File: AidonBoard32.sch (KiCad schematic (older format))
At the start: 30 parts, among them J1 RJ12, M1 MICRO_USB_18_TH, Q1 S8050, Q2 S8050, U1 AMS1117-3V3, U2 CP2102N-GQFN24, U3 ESP32-WROOM, U4 74HC04D

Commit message: Finished first revision of AidonBoard32!
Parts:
- added D6: 1N5819, Diode_SMD:D_SOD-123F, symbol Diode:1N5819
- D1: value 1N5819/SS14 -> 1N5819
- U4: footprint Package_SO:SO-14_3.9x8.65mm_P1.27mm -> Package_SO:SOIC-14_3.9x8.7mm_P1.27mm
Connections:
- net labels added: +5V, HAN_OUT, VDD
- net labels removed: UART_TX
- wire segments 128 -> 147
- no-connect marks 37 -> 50
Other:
- note added: "ESP32 Flashing"
- note added: "LEDs"
- note added: "P1 Port"
- note added: "RJ11 Connector"
- note removed: "HAN Port - UART"
- note removed: "LED"
- note removed: "Programming"
- note removed: "RJ Connector"
- moved on the sheet: C1, C10, C2, C3, C4, C5, C6, C7, D2, D3, D4, D5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

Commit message: Update
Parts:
- removed D1, D6: 1N5819, Diode_SMD:D_SOD-123F, symbol Diode:1N5819
- removed U4: 74HC04D, Package_SO:SOIC-14_3.9x8.7mm_P1.27mm, symbol Henrik-IC-Inverters:74HC04D
- added D1: SS54, Diode_SMD:D_SMA, symbol Diode:B120-E3
- added D5: LED_Small, LED_SMD:LED_0603_1608Metric_Pad1.05x0.95mm_HandSolder, symbol Device:LED_Small
- added Q1: Si2301CDS-T1-GE3, Package_TO_SOT_SMD:SOT-23_Handsoldering, symbol Device:Q_PMOS_GSD
- added Q4: MMBT3904, Package_TO_SOT_SMD:SOT-23_Handsoldering, symbol Transistor_BJT:MMBT3904
- added R1: 100K, Resistor_SMD:R_0603_1608Metric_Pad0.98x0.95mm_HandSolder, symbol Device:R_Small
- added R10, R12: 10K, Resistor_SMD:R_0603_1608Metric_Pad0.98x0.95mm_HandSolder, symbol Device:R_Small
- added R11: 1K, Resistor_SMD:R_0603_1608Metric_Pad0.98x0.95mm_HandSolder, symbol Device:R_Small
- added R9: 220, Resistor_SMD:R_0603_1608Metric_Pad0.98x0.95mm_HandSolder, symbol Device:R_Small
- C1, C2: Description (none) -> Power Regulator Capacitors; LCSC (none) -> C231297
- C10: renamed from C7; footprint Capacitor_SMD:C_1206_3216Metric_Pad1.33x1.80mm_HandSolder -> Capacitor_SMD:C_0603_1608Metric_Pad1.08x0.95mm_HandSolder; Description (none) -> Various Capacitors; LCSC (none) -> C478888
- C3, C5: Description (none) -> CP2102N Capacitors; LCSC (none) -> C129235
- C4, C6: footprint Capacitor_SMD:C_1206_3216Metric_Pad1.33x1.80mm_HandSolder -> Capacitor_SMD:C_0603_1608Metric_Pad1.08x0.95mm_HandSolder; Description (none) -> Various Capacitors; LCSC (none) -> C478888
- C7: renamed from C8; value 47uF -> 10uF; Description (none) -> ESP32 VDD Capacitor; LCSC (none) -> C119052
- C8: renamed from C9; footprint Capacitor_SMD:C_1206_3216Metric_Pad1.33x1.80mm_HandSolder -> Capacitor_SMD:C_0603_1608Metric_Pad1.08x0.95mm_HandSolder; Description (none) -> Various Capacitors; LCSC (none) -> C478888
- C9: renamed from C10; value 10uF -> 1uF; Description (none) -> ESP32 EN PIN Capacitor; LCSC (none) -> C123716
- D2: footprint LED_SMD:LED_1206_3216Metric_Pad1.42x1.75mm_HandSolder -> LED_SMD:LED_0603_1608Metric_Pad1.05x0.95mm_HandSolder; Description (none) -> TX LED / Blue; LCSC (none) -> C273617
- D3: footprint LED_SMD:LED_1206_3216Metric_Pad1.42x1.75mm_HandSolder -> LED_SMD:LED_0603_1608Metric_Pad1.05x0.95mm_HandSolder; Description (none) -> RX LED / Yellow; LCSC (none) -> C192668
- D4: footprint LED_SMD:LED_1206_3216Metric_Pad1.42x1.75mm_HandSolder -> LED_SMD:LED_0603_1608Metric_Pad1.05x0.95mm_HandSolder; Description (none) -> Power LED / Red; LCSC (none) -> C192315
- D6: renamed from D5; Description (none) -> RGB LED; LCSC (none) -> C114586
- J1: footprint Henrik-Connectors:RJ11-6 -> 5555165-1:TE_5555165-1; Description (none) -> RJ12 Connector; LCSC (none) -> C305981
- M1: value MICRO_USB_18_TH -> U-F-M5DD-Y-L; Description (none) -> Micro USB Connector; LCSC (none) -> C91146
- Q2: renamed from Q1; value S8050 -> MMBT3904; LCSC (none) -> C20526
- Q3: renamed from Q2; value S8050 -> MMBT3904; LCSC (none) -> C20526
- R2: renamed from R1; value 1k -> 1K; footprint Resistor_SMD:R_1206_3216Metric_Pad1.30x1.75mm_HandSolder -> Resistor_SMD:R_0603_1608Metric_Pad0.98x0.95mm_HandSolder; LCSC (none) -> C491209
- R3: renamed from R7; value 1k -> 10K; footprint Resistor_SMD:R_1206_3216Metric_Pad1.30x1.75mm_HandSolder -> Resistor_SMD:R_0603_1608Metric_Pad0.98x0.95mm_HandSolder; LCSC (none) -> C510087
- R4: renamed from R5; value 12k -> 10K; footprint Resistor_SMD:R_1206_3216Metric_Pad1.30x1.75mm_HandSolder -> Resistor_SMD:R_0603_1608Metric_Pad0.98x0.95mm_HandSolder; LCSC (none) -> C510087
- R5: renamed from R6; value 12k -> 10K; footprint Resistor_SMD:R_1206_3216Metric_Pad1.30x1.75mm_HandSolder -> Resistor_SMD:R_0603_1608Metric_Pad0.98x0.95mm_HandSolder; LCSC (none) -> C510087
- R6: renamed from R2; value 1k -> 220; footprint Resistor_SMD:R_1206_3216Metric_Pad1.30x1.75mm_HandSolder -> Resistor_SMD:R_0603_1608Metric_Pad0.98x0.95mm_HandSolder; Description (none) -> LED Resistors; LCSC (none) -> C441917
- R7: renamed from R3; value 1k -> 220; footprint Resistor_SMD:R_1206_3216Metric_Pad1.30x1.75mm_HandSolder -> Resistor_SMD:R_0603_1608Metric_Pad0.98x0.95mm_HandSolder; Description (none) -> LED Resistors; LCSC (none) -> C441917
- R8: renamed from R4; value 1k -> 220; footprint Resistor_SMD:R_1206_3216Metric_Pad1.30x1.75mm_HandSolder -> Resistor_SMD:R_0603_1608Metric_Pad0.98x0.95mm_HandSolder; Description (none) -> LED Resistors; LCSC (none) -> C441917
- U1: LCSC (none) -> C6186
- U2: LCSC (none) -> C1550551
- U3: LCSC (none) -> C82899
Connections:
- net labels added: VCC
- net labels removed: VDD
- wire segments 147 -> 156
- no-connect marks 50 -> 39
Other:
- note added: "P1 Signal Inversion"
- note removed: "P1 Port"
- moved on the sheet: C1, C2, D2, D3, D4, Q2, Q3, R6, R7, R8, U1

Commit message: Fixed routing
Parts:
- J1: symbol Connector:RJ12 -> AidonBoard32-rescue:RJ12-Connector
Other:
- moved on the sheet: R6, R7, R8, R9
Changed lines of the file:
@@
 $EndComp
-Wire Wire Line
-	9450 2350 9450 2100
-Wire Wire Line
-	9450 1900 9450 1800
 Wire Wire Line
 	9450 2350 9650 2350
@@
 $EndComp
 $Comp
-L Connector:RJ12 J1
+L AidonBoard32-rescue:RJ12-Connector J1
 U 1 1 608CEFE8
 P 4250 4300
@@
 $EndComp
 $Comp
-L Device:R_Small R10
-U 1 1 60C4F049
-P 9450 2000
-F 0 "R10" H 9456 2123 50  0000 L CNN
-F 1 "10K" H 9459 1889 50  0000 L CNN
-F 2 "Resistor_SMD:R_0603_1608Metric_Pad0.98x0.95mm_HandSolder" H 9450 2000 50  0001 C CNN
-F 3 "https://datasheet.lcsc.com/lcsc/2004232132_ROHM-Semicon-ESR03EZPF1002_C510087.pdf" H 9450 2000 50  0001 C CNN
-F 4 "C510087" H 9450 2000 50  0001 C CNN "LCSC"
-	1    9450 2000
-	1    0    0    -1
-$EndComp
-$Comp
 L Device:R_Small R11
 U 1 1 60C63B88
@@
 L Device:R_Small R8
 U 1 1 5AAA8BC7
-P 9250 4450
-F 0 "R8" V 9176 4403 50  0000 L CNN
-F 1 "220" V 9325 4377 50  0000 L CNN
-F 2 "Resistor_SMD:R_0603_1608Metric_Pad0.98x0.95mm_HandSolder" H 9250 4450 50  0001 C CNN
-F 3 "" H 9250 4450 50  0001 C CNN
-F 4 "C441917" H 9250 4450 50  0001 C CNN "LCSC"
-F 5 "LED Resistors" H 9250 4450 50  0001 C CNN "Description"
-	1    9250 4450
-	0    1    1    0
-$EndComp
-Wire Wire Line
-	9500 4450 9350 4450
-Wire Wire Line
-	9050 4450 9150 4450
+P 9200 4450
+F 0 "R8" V 9126 4403 50  0000 L CNN
+F 1 "220" V 9275 4377 50  0000 L CNN
+F 2 "Resistor_SMD:R_0603_1608Metric_Pad0.98x0.95mm_HandSolder" H 9200 4450 50  0001 C CNN
+F 3 "" H 9200 4450 50  0001 C CNN
+F 4 "C441917" H 9200 4450 50  0001 C CNN "LCSC"
+F 5 "LED Resistors" H 9200 4450 50  0001 C CNN "Description"
+	1    9200 4450
+	0    1    1    0
+$EndComp
+Wire Wire Line
+	9450 4450 9300 4450
+Wire Wire Line
+	9050 4450 9100 4450
 $Comp
 L Device:LED_Small D4
@@
 L Device:R_Small R9
 U 1 1 60FFD57F
-P 9250 4700
-F 0 "R9" V 9173 4653 50  0000 L CNN
-F 1 "220" V 9328 4637 50  0000 L CNN
-F 2 "Resistor_SMD:R_0603_1608Metric_Pad0.98x0.95mm_HandSolder" H 9250 4700 50  0001 C CNN
-F 3 "" H 9250 4700 50  0001 C CNN
-F 4 "C441917" H 9250 4700 50  0001 C CNN "LCSC"
-F 5 "LED Resistors" H 9250 4700 50  0001 C CNN "Description"
-	1    9250 4700
-	0    1    1    0
-$EndComp
-Wire Wire Line
-	9050 4700 9150 4700
-Wire Wire Line
-	9500 4700 9350 4700
+P 9200 4700
+F 0 "R9" V 9123 4653 50  0000 L CNN
+F 1 "220" V 9278 4637 50  0000 L CNN
+F 2 "Resistor_SMD:R_0603_1608Metric_Pad0.98x0.95mm_HandSolder" H 9200 4700 50  0001 C CNN
+F 3 "" H 9200 4700 50  0001 C CNN
+F 4 "C441917" H 9200 4700 50  0001 C CNN "LCSC"
+F 5 "LED Resistors" H 9200 4700 50  0001 C CNN "Description"
+	1    9200 4700
+	0    1    1    0
+$EndComp
+Wire Wire Line
+	9050 4700 9100 4700
+Wire Wire Line
+	9450 4700 9300 4700
 $Comp
 L Device:LED_Small D3
@@
 $EndComp
 $Comp
+L Device:R_Small R7
+U 1 1 5AAA8B96
+P 9200 4200
+F 0 "R7" V 9125 4148 50  0000 L CNN
+F 1 "220" V 9267 4132 50  0000 L CNN
+F 2 "Resistor_SMD:R_0603_1608Metric_Pad0.98x0.95mm_HandSolder" H 9200 4200 50  0001 C CNN
+F 3 "" H 9200 4200 50  0001 C CNN
+F 4 "C441917" H 9200 4200 50  0001 C CNN "LCSC"
+F 5 "LED Resistors" H 9200 4200 50  0001 C CNN "Description"
+	1    9200 4200
+	0    1    1    0
+$EndComp
+$Comp
+L Device:R_Small R6
+U 1 1 5AAA89A6
+P 9200 3950
+F 0 "R6" V 9128 3898 50  0000 L CNN
+F 1 "220" V 9272 3885 50  0000 L CNN
+F 2 "Resistor_SMD:R_0603_1608Metric_Pad0.98x0.95mm_HandSolder" H 9200 3950 50  0001 C CNN
+F 3 "" H 9200 3950 50  0001 C CNN
+F 4 "C441917" H 9200 3950 50  0001 C CNN "LCSC"
+F 5 "LED Resistors" H 9200 3950 50  0001 C CNN "Description"
+	1    9200 3950
+	0    1    1    0
+$EndComp
+Wire Wire Line
+	10050 4700 10000 4700
+Wire Wire Line
+	9050 4200 9100 4200
+Wire Wire Line
+	9050 3950 9100 3950
+Wire Wire Line
+	9450 4200 9300 4200
+Wire Wire Line
+	9300 3950 9450 3950
+$Comp
+L power:+3.3V #PWR023
+U 1 1 5AAA9570
+P 8700 4300
+F 0 "#PWR023" H 8700 4150 50  0001 C CNN
+F 1 "+3.3V" H 8700 4440 50  0000 C CNN
+F 2 "" H 8700 4300 50  0001 C CNN
+F 3 "" H 8700 4300 50  0001 C CNN
+	1    8700 4300
+	1    0    0    -1
+$EndComp
+Text Label 9450 4200 0    60   ~ 0
+LED_RX
+Text Label 9450 3950 0    60   ~ 0
+LED_TX
+Connection ~ 8850 4200
+Wire Wire Line
+	8850 4200 8850 4450
+Wire Notes Line
+	8500 5000 11100 5000
+Wire Wire Line
+	9450 4700 9450 4450
+Connection ~ 9450 4700
+Wire Wire Line
+	9450 4700 9450 4750
+$Comp
+L power:GND #PWR0101
+U 1 1 60FFD575
+P 9450 4750
+F 0 "#PWR0101" H 9450 4500 50  0001 C CNN
+F 1 "GND" H 9450 4600 50  0000 C CNN
+F 2 "" H 9450 4750 50  0001 C CNN
+F 3 "" H 9450 4750 50  0001 C CNN
+	1    9450 4750
+	1    0    0    -1
+$EndComp
+Wire Wire Line
+	1850 4400 2050 4400
+Connection ~ 2050 4400
+Wire Wire Line
+	2050 4400 2100 4400
+$Comp
+L power:VCC #PWR0103
+U 1 1 610B3EF6
+P 10000 4700
+F 0 "#PWR0103" H 10000 4550 50  0001 C CNN
+F 1 "VCC" H 10000 4850 50  0000 C CNN
+F 2 "" H 10000 4700 50  0001 C CNN
+F 3 "" H 10000 4700 50  0001 C CNN
+	1    10000 4700
+	0    -1   -1   0
+$EndComp
+Wire Wire Line
+	2000 4350 2050 4400
+$Comp
+L power:VCC #PWR0102
+U 1 1 610A4F64
+P 2000 4350
+F 0 "#PWR0102" H 2000 4200 50  0001 C CNN
+F 1 "VCC" H 2000 4500 50  0000 C CNN
+F 2 "" H 2000 4350 50  0001 C CNN
+F 3 "" H 2000 4350 50  0001 C CNN
+	1    2000 4350
+	1    0    0    -1
+$EndComp
+$Comp
 L Device:LED_Small D2
 U 1 1 5AAA92A7
@@
 	-1   0    0    1
 $EndComp
-$Comp
-L Device:R_Small R7
-U 1 1 5AAA8B96
-P 9250 4200
-F 0 "R7" V 9175 4148 50  0000 L CNN
-F 1 "220" V 9317 4132 50  0000 L CNN
-F 2 "Resistor_SMD:R_0603_1608Metric_Pad0.98x0.95mm_HandSolder" H 9250 4200 50  0001 C CNN
-F 3 "" H 9250 4200 50  0001 C CNN
-F 4 "C441917" H 9250 4200 50  0001 C CNN "LCSC"
-F 5 "LED Resistors" H 9250 4200 50  0001 C CNN "Description"
-	1    9250 4200
-	0    1    1    0
-$EndComp
-$Comp
-L Device:R_Small R6
-U 1 1 5AAA89A6
-P 9250 3950
-F 0 "R6" V 9178 3898 50  0000 L CNN
-F 1 "220" V 9322 3885 50  0000 L CNN
-F 2 "Resistor_SMD:R_0603_1608Metric_Pad0.98x0.95mm_HandSolder" H 9250 3950 50  0001 C CNN
-F 3 "" H 9250 3950 50  0001 C CNN
-F 4 "C441917" H 9250 3950 50  0001 C CNN "LCSC"
-F 5 "LED Resistors" H 9250 3950 50  0001 C CNN "Description"
-	1    9250 3950
-	0    1    1    0
-$EndComp
-Wire Wire Line
-	10050 4700 10000 4700
-Wire Wire Line
-	9050 4200 9150 4200
-Wire Wire Line
-	9050 3950 9150 3950
-Wire Wire Line
-	9500 4200 9350 4200
-Wire Wire Line
-	9350 3950 9500 3950
-$Comp
-L power:+3.3V #PWR023
-U 1 1 5AAA9570
-P 8700 4300
-F 0 "#PWR023" H 8700 4150 50  0001 C CNN
-F 1 "+3.3V" H 8700 4440 50  0000 C CNN
-F 2 "" H 8700 4300 50  0001 C CNN
-F 3 "" H 8700 4300 50  0001 C CNN
-	1    8700 4300
-	1    0    0    -1
-$EndComp
-Text Label 9500 4200 0    60   ~ 0
-LED_RX
-Text Label 9500 3950 0    60   ~ 0
-LED_TX
-Connection ~ 8850 4200
-Wire Wire Line
-	8850 4200 8850 4450
-Wire Notes Line
-	8500 5000 11100 5000
-Wire Wire Line
-	9500 4700 9500 4450
-Connection ~ 9500 4700
-Wire Wire Line
-	9500 4700 9500 4750
-$Comp
-L power:GND #PWR0101
-U 1 1 60FFD575
-P 9500 4750
-F 0 "#PWR0101" H 9500 4500 50  0001 C CNN
-F 1 "GND" H 9500 4600 50  0000 C CNN
-F 2 "" H 9500 4750 50  0001 C CNN
-F 3 "" H 9500 4750 50  0001 C CNN
-	1    9500 4750
-	1    0    0    -1
-$EndComp
-Wire Wire Line
-	1850 4400 2050 4400
-Connection ~ 2050 4400
-Wire Wire Line
-	2050 4400 2100 4400
-$Comp
-L power:VCC #PWR0103
-U 1 1 610B3EF6
-P 10000 4700
-F 0 "#PWR0103" H 10000 4550 50  0001 C CNN
-F 1 "VCC" H 10000 4850 50  0000 C CNN
-F 2 "" H 10000 4700 50  0001 C CNN
-F 3 "" H 10000 4700 50  0001 C CNN
-	1    10000 4700
-	0    -1   -1   0
-$EndComp
-Wire Wire Line
-	2000 4350 2050 4400
-$Comp
-L power:VCC #PWR0102
-U 1 1 610A4F64
-P 2000 4350
-F 0 "#PWR0102" H 2000 4200 50  0001 C CNN
-F 1 "VCC" H 2000 4500 50  0000 C CNN
-F 2 "" H 2000 4350 50  0001 C CNN
-F 3 "" H 2000 4350 50  0001 C CNN
-	1    2000 4350
-	1    0    0    -1
-$EndComp
+Wire Wire Line
+	9450 2350 9450 2100
+Wire Wire Line
+	9450 1900 9450 1800
+$Comp
+L Device:R_Small R10
+U 1 1 60C4F049
+P 9450 2000
+F 0 "R10" H 9456 2123 50  0000 L CNN
+F 1 "10K" H 9459 1889 50  0000 L CNN
+F 2 "Resistor_SMD:R_0603_1608Metric_Pad0.98x0.95mm_HandSolder" H 9450 2000 50  0001 C CNN
+F 3 "https://datasheet.lcsc.com/lcsc/2004232132_ROHM-Semicon-ESR03EZPF1002_C510087.pdf" H 9450 2000 50  0001 C CNN
+F 4 "C510087" H 9450 2000 50  0001 C CNN "LCSC"
+	1    9450 2000
+	1    0    0    -1
+$EndComp

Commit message: Fixed small issues
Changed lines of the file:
@@
 $EndComp
 Wire Wire Line
-	1850 4400 2050 4400
-Connection ~ 2050 4400
+	1850 4400 2000 4400
+Connection ~ 2000 4400
 Wire Wire Line
-	2050 4400 2100 4400
+	2000 4400 2100 4400
 $Comp
 L power:VCC #PWR0103
@@
 $EndComp
 Wire Wire Line
-	2000 4350 2050 4400
+	2000 4350 2000 4400
 $Comp
 L power:VCC #PWR0102

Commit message: Updates
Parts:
- J1: symbol AidonBoard32-rescue:RJ12-Connector -> Connector:RJ12
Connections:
- net +3V3: now also D2.2 (A), D3.2 (A), D4.2 (A), D5.2 (A)
- net GND: no longer U2.25 (GND), U3.39 (GND-PAD)
- no-connect marks 39 -> 41
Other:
- moved on the sheet: C1, C2, D1, R10

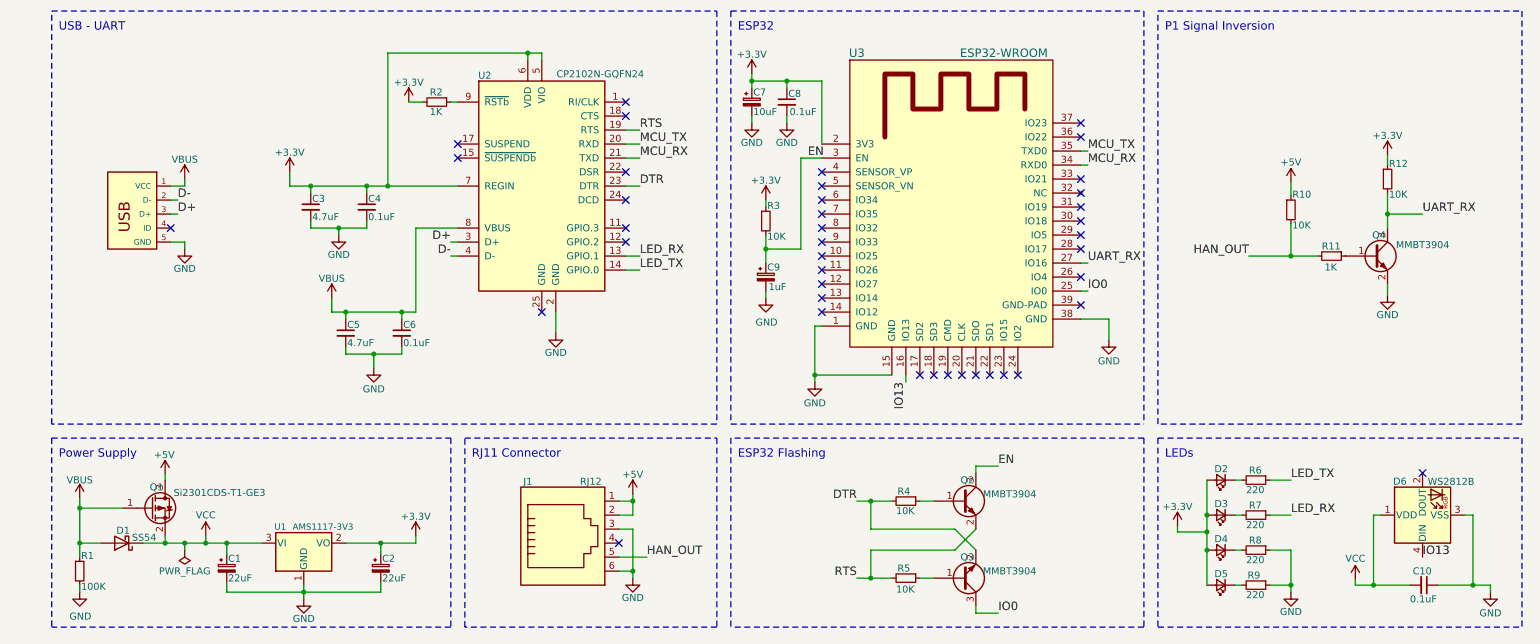
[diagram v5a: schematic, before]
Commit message: Updated some component values in schematic
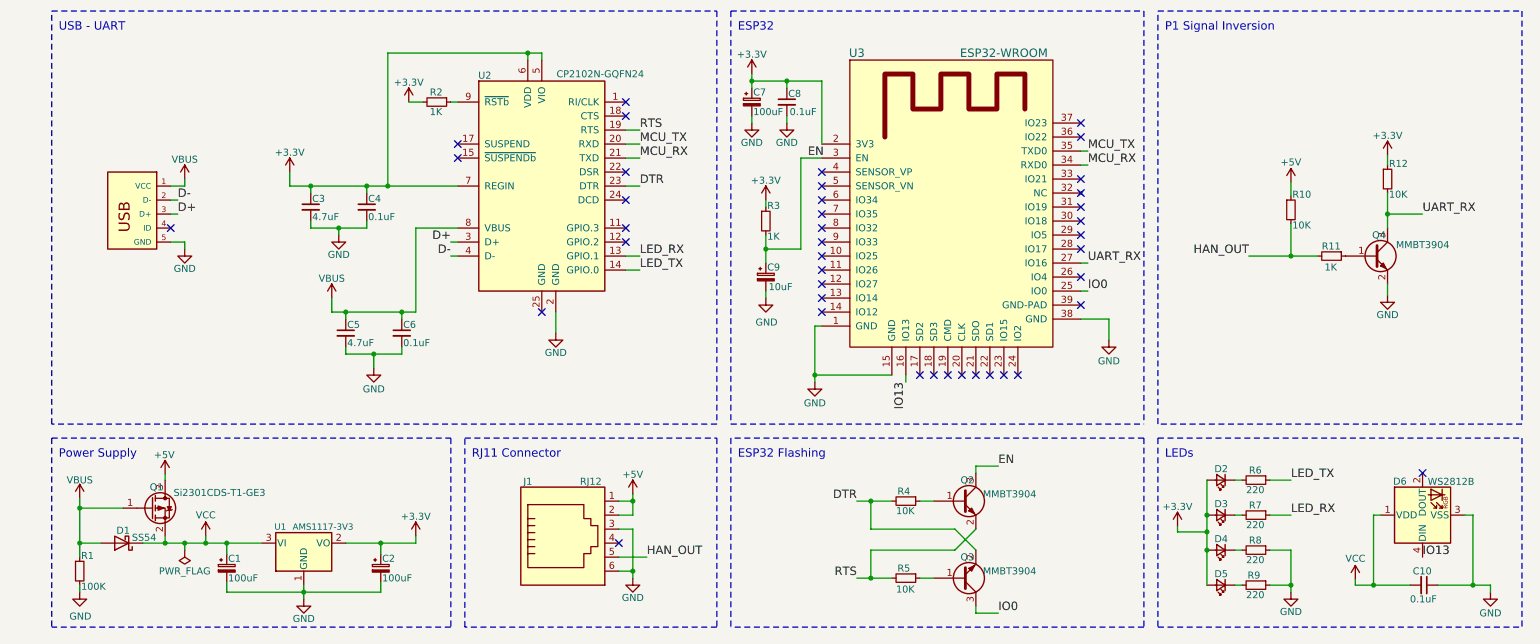
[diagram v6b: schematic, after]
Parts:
- C1, C2: value 22uF -> 100uF
- C7: value 10uF -> 100uF
- C9: value 1uF -> 10uF
- R3: value 10K -> 1K
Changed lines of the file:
@@
 Sheet 1 1
 Title "AidonBoard32"
-Date "2021-04-30"
-Rev "2"
+Date "2021-05-13"
+Rev "3"
 Comp "Henrik Nelson"
 Comment1 ""
@@
 P 2950 4580
 F 0 "C2" H 2960 4650 50  0000 L CNN
-F 1 "22uF" H 2960 4510 50  0000 L CNN
+F 1 "100uF" H 2960 4510 50  0000 L CNN
 F 2 "Capacitor_SMD:C_1206_3216Metric_Pad1.33x1.80mm_HandSolder" H 2950 4580 50  0001 C CNN
 F 3 "" H 2950 4580 50  0001 C CNN
@@
 P 1850 4580
 F 0 "C1" H 1860 4650 50  0000 L CNN
-F 1 "22uF" H 1860 4510 50  0000 L CNN
+F 1 "100uF" H 1860 4510 50  0000 L CNN
 F 2 "Capacitor_SMD:C_1206_3216Metric_Pad1.33x1.80mm_HandSolder" H 1850 4580 50  0001 C CNN
 F 3 "" H 1850 4580 50  0001 C CNN
@@
 P 5700 2100
 F 0 "R3" H 5710 2210 50  0000 L CNN
-F 1 "10K" H 5710 1990 50  0000 L CNN
+F 1 "1K" H 5710 1990 50  0000 L CNN
 F 2 "Resistor_SMD:R_0603_1608Metric_Pad0.98x0.95mm_HandSolder" H 5700 2100 50  0001 C CNN
 F 3 "https://datasheet.lcsc.com/lcsc/2004232132_ROHM-Semicon-ESR03EZPF1002_C510087.pdf" H 5700 2100 50  0001 C CNN
@@
 P 5700 2500
 F 0 "C9" H 5710 2570 50  0000 L CNN
-F 1 "1uF" H 5720 2430 50  0000 L CNN
+F 1 "10uF" H 5720 2430 50  0000 L CNN
 F 2 "Capacitor_SMD:C_1206_3216Metric_Pad1.33x1.80mm_HandSolder" H 5700 2500 50  0001 C CNN
 F 3 "https://datasheet.lcsc.com/lcsc/1808272318_KEMET-T491A105K025AT_C123716.pdf" H 5700 2500 50  0001 C CNN
@@
 P 5600 1250
 F 0 "C7" H 5610 1320 50  0000 L CNN
-F 1 "10uF" H 5610 1180 50  0000 L CNN
+F 1 "100uF" H 5610 1180 50  0000 L CNN
 F 2 "Capacitor_SMD:C_1206_3216Metric_Pad1.33x1.80mm_HandSolder" H 5600 1250 50  0001 C CNN
 F 3 "https://datasheet.lcsc.com/lcsc/Hunan-Xiangyee-in-S-T-CA45-A010K106T_C119052.pdf" H 5600 1250 50  0001 C CNN
